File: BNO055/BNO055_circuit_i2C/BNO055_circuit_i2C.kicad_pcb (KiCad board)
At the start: 2 copper layers, 27.8 x 9.3 mm, 11 parts, among them U1 BNO055

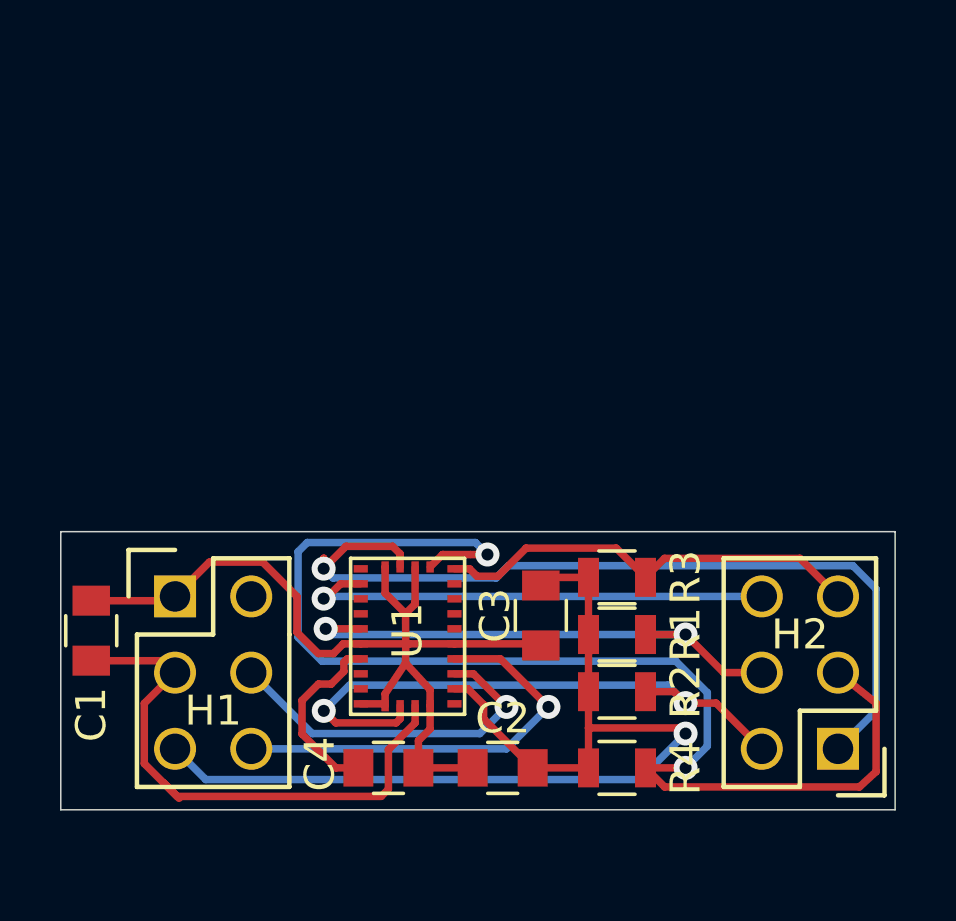
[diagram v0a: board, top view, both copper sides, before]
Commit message: redesign BNO055 breakout, except for small changes
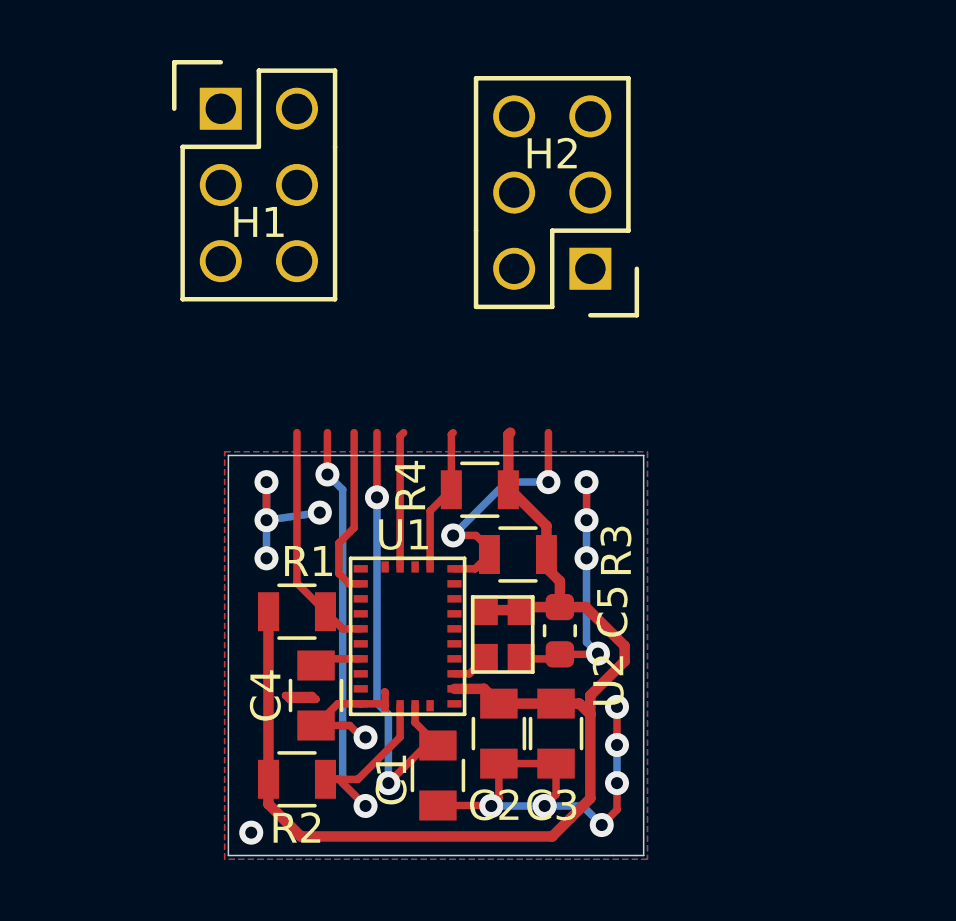
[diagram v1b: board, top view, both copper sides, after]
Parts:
- added C5: 0.01u, footprints:C_0603_1608Metric, F.Cu at (155.6, 90.0)
- added U2: ASDMB-xxxMHz, ASDK2-32.768KHZ-LR-T3:ASDK2-32.768KHZ-LR-T3, F.Cu at (153.7, 90.2)
- moved H2 18.0 mm to (156.6, 78.0)
- moved H1 16.3 mm to (144.3, 72.6)
- moved C1 12.5 mm to (151.5, 94.9), turned to 270 degrees
- moved R2 11.1 mm to (146.8, 95.0)
- moved R1 10.7 mm to (146.8, 89.4)
- moved R4 10.3 mm to (152.9, 85.3), turned to 180 degrees
- moved C3 3.97 mm to (155.4, 93.5)
- moved C4 3.41 mm to (147.4, 92.2), turned to 270 degrees
- moved R3 3.39 mm to (154.2, 87.5), turned to 180 degrees
- moved C2 1.15 mm to (153.5, 93.5), turned to 90 degrees
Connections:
- H1 pad 4: OptionalOSCinput -> Net-(H1-Pad4)
- H1 pad 6: OptionalOSCoutput -> Net-(H1-Pad6)
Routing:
- net SCL: track 42.2 -> 4.80 mm, vias 2 -> 0
- net COM3: track 28.7 -> 4.53 mm, vias 1 -> 0
- net OptionalOSCoutput: track 14.3 -> 0.00 mm, vias 1 -> 0
- net OptionalOSCinput: track 11.9 -> 1.20 mm, vias 1 -> 0
- net INT: track 16.1 -> 5.78 mm, vias 1 -> 0
- net nRESET: track 17.6 -> 7.77 mm, vias 2 -> 0
- net SDA: track 14.5 -> 8.51 mm, vias 0 -> 2
- net GND: track 31.6 -> 36.3 mm, vias 0 -> 16
- net VDDIO: track 35.4 -> 40.1 mm, vias 1 -> 0
- net Net-(C4-Pad1): track 6.18 -> 1.58 mm
- net VDD: track 19.1 -> 15.7 mm, vias 0 -> 2
- net nBOOT_LOAD_PIN: track 20.5 -> 18.8 mm
- added copper zone on B.Cu, net GND
- added copper zone on F.Cu, net GND
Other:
- board size 27.8 x 9.3 mm -> 13.8 x 13.3 mm
- net class VDDIO added: clearance 0.2, trace_width 0.35, via_dia 1, via_drill 0.4
